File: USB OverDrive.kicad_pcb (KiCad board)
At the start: 4 copper layers, 30.3 x 50 mm, 90 parts, among them J5 USB_A, J6 USB_A, J7 USB_A, P2 USB_C_Plug_USB2.0, U1 5.0V, U2 3.3V, U3 TPS2561, U4 TPS2561, U5 1.2V, U7 TUSB4041I, Y1 Crystal_GND24

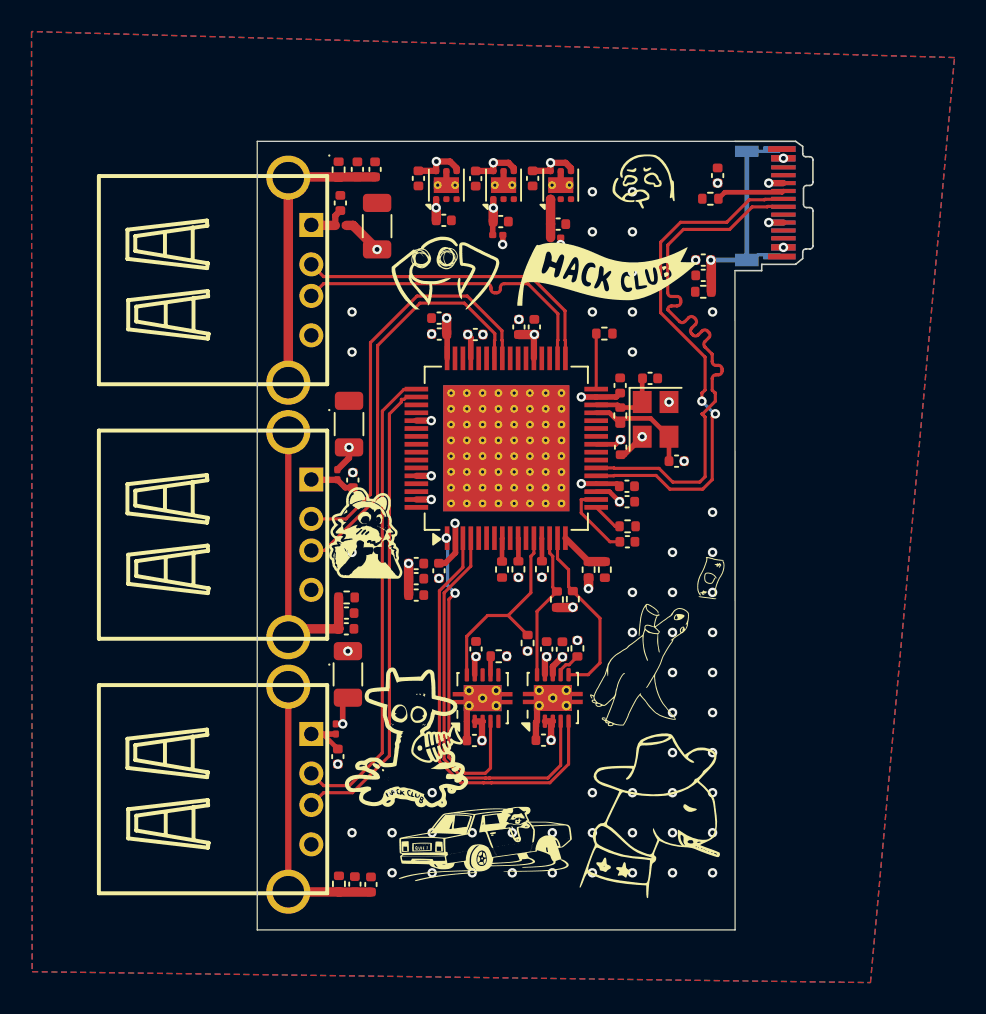
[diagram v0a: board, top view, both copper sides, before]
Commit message: add qr
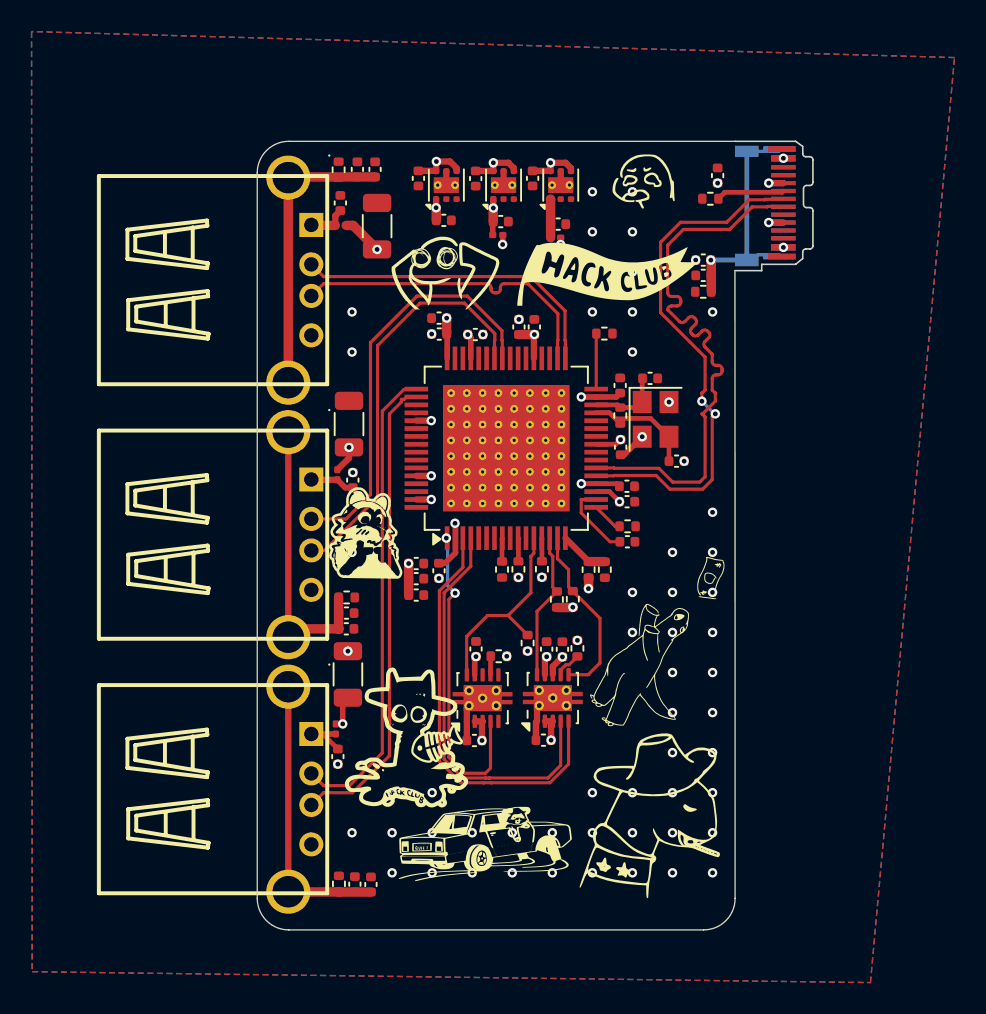
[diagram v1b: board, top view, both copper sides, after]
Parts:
- added G***: LOGO, LOGO, B.Cu at (132.7, 100.2)
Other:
- outline, holes or cut-outs redrawn
